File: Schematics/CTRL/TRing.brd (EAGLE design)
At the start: 94 x 49.2 mm, 39 parts

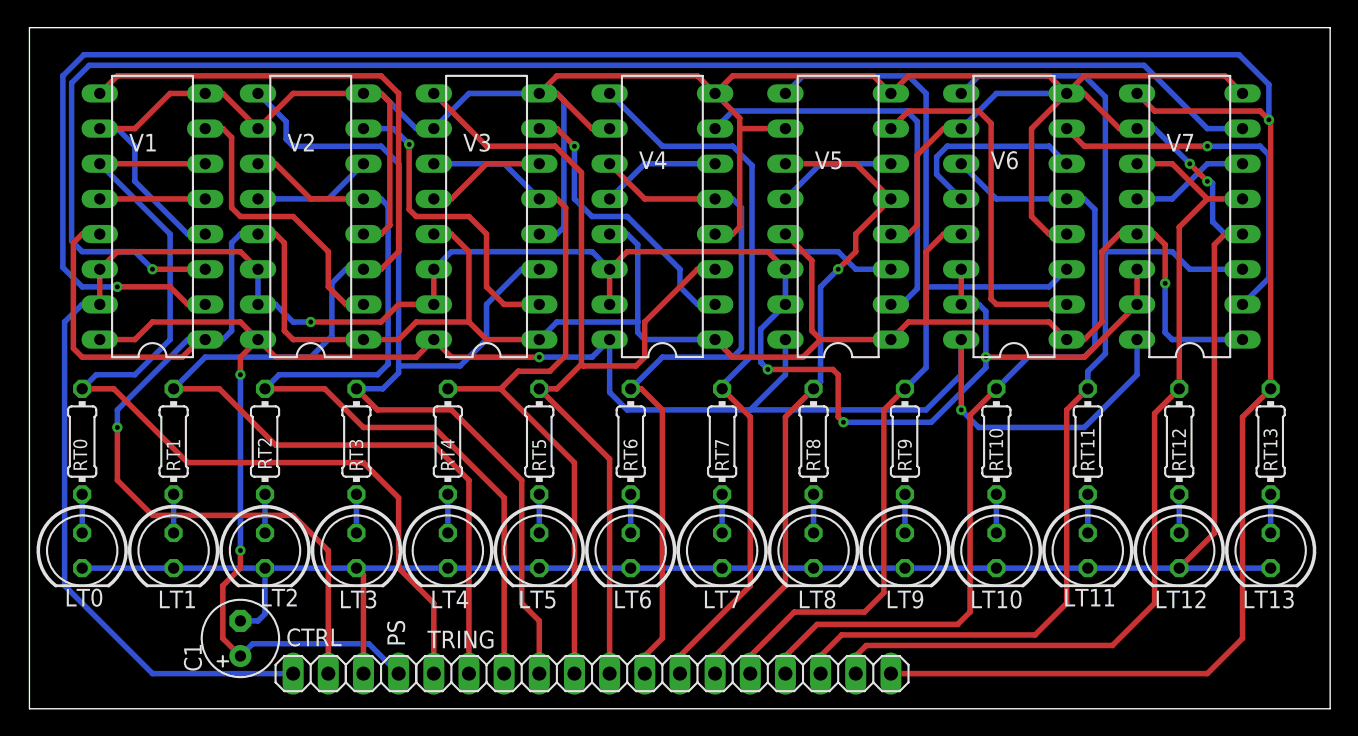
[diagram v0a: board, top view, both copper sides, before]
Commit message: Reduce Tring width
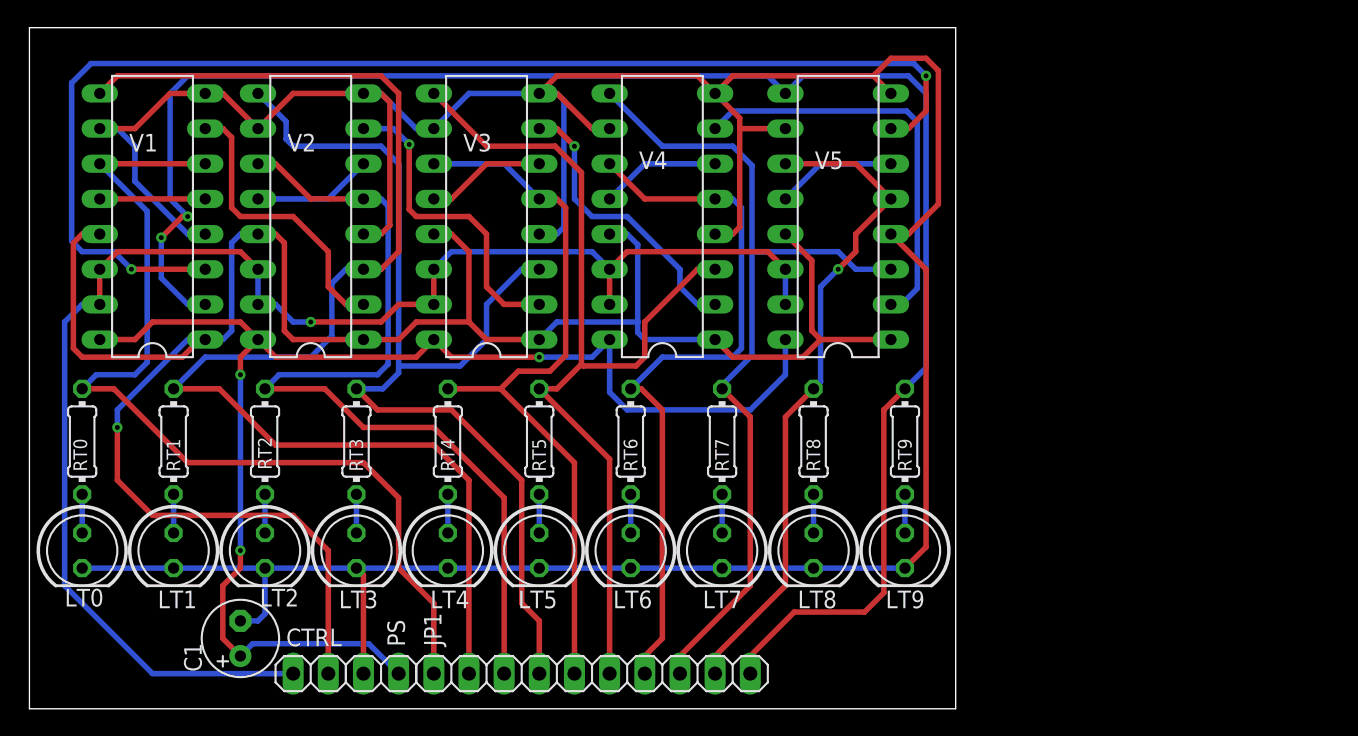
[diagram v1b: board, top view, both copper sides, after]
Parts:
- removed LT10, LT11, LT12, LT13: (no value), led:LED5MM
- removed RT10, RT11, RT12, RT13: (no value), rcl:0204/7
- removed TRING: (no value), pinhead:1X14
- removed V6, V7: 74112N, 74ttl-din:DIL16
- added JP1: (no value), pinhead:1X10
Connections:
- removed net !T13: V1.3, V7.7
- removed net N$12: V5.7, V6.2
- removed net N$14: V6.12, V6.6
- removed net N$20: LT10.A, RT10.1
- removed net N$21: LT11.A, RT11.1
- removed net N$22: V6.7, V7.2
- removed net N$24: LT12.A, RT12.1
- removed net N$25: V7.12, V7.6
- removed net N$26: LT13.A, RT13.1
- removed net T10: RT10.2, TRING.11, V6.11, V6.5
- removed net T11: RT11.2, TRING.12, V6.9, V7.3
- removed net T12: RT12.2, TRING.13, V7.11, V7.5
- removed net T13: RT13.2, TRING.14, V1.2, V7.9
- new net !T9: V1.3, V5.7
- net CLK: no longer V6.1, V6.13, V7.1, V7.13
- net CLR: no longer V6.14, V6.15, V7.14, V7.15
- net GND: no longer LT10.K, LT11.K, LT12.K, LT13.K, V6.10, V6.4, V6.8, V7.10, V7.4, V7.8
- net T0: now also JP1.10; no longer TRING.1
- net T1: now also JP1.9; no longer TRING.2
- net T2: now also JP1.8; no longer TRING.3
- net T3: now also JP1.7; no longer TRING.4
- net T4: now also JP1.6; no longer TRING.5
- net T5: now also JP1.5; no longer TRING.6
- net T6: now also JP1.4; no longer TRING.7
- net T7: now also JP1.3; no longer TRING.8
- net T8: now also JP1.2; no longer TRING.9
- net T9: now also JP1.1, V1.2; no longer TRING.10, V6.3
- net VCC: no longer V6.16, V7.16
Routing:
- net T13: track 191.5 -> 0.00 mm, vias 2 -> 0
- net !T13: track 108.9 -> 0.00 mm, vias 1 -> 0
- net !T9: track 0.00 -> 90.2 mm, vias 0 -> 2
- net GND: track 329.6 -> 242.9 mm, vias 2 -> 0
- net T11: track 80.4 -> 0.00 mm
- net T12: track 63.9 -> 0.00 mm
- net T10: track 62.1 -> 0.00 mm
- net T9: track 72.0 -> 125.7 mm, vias 0 -> 2
- net CLR: track 157.7 -> 107.7 mm, vias 4 -> 1
- net CLK: track 199.1 -> 151.5 mm, vias 2 -> 1
- net VCC: track 139.0 -> 97.7 mm, vias 4 -> 3
- net N$22: track 27.0 -> 0.00 mm, vias 1 -> 0
- net N$12: track 26.5 -> 0.00 mm
- net N$14: track 14.0 -> 0.00 mm
- net N$25: track 8.67 -> 0.00 mm
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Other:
- board size 94 x 49.2 mm -> 66.9 x 49.2 mm

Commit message: Changed order of LEDs and widht is now 11bits (0-10).
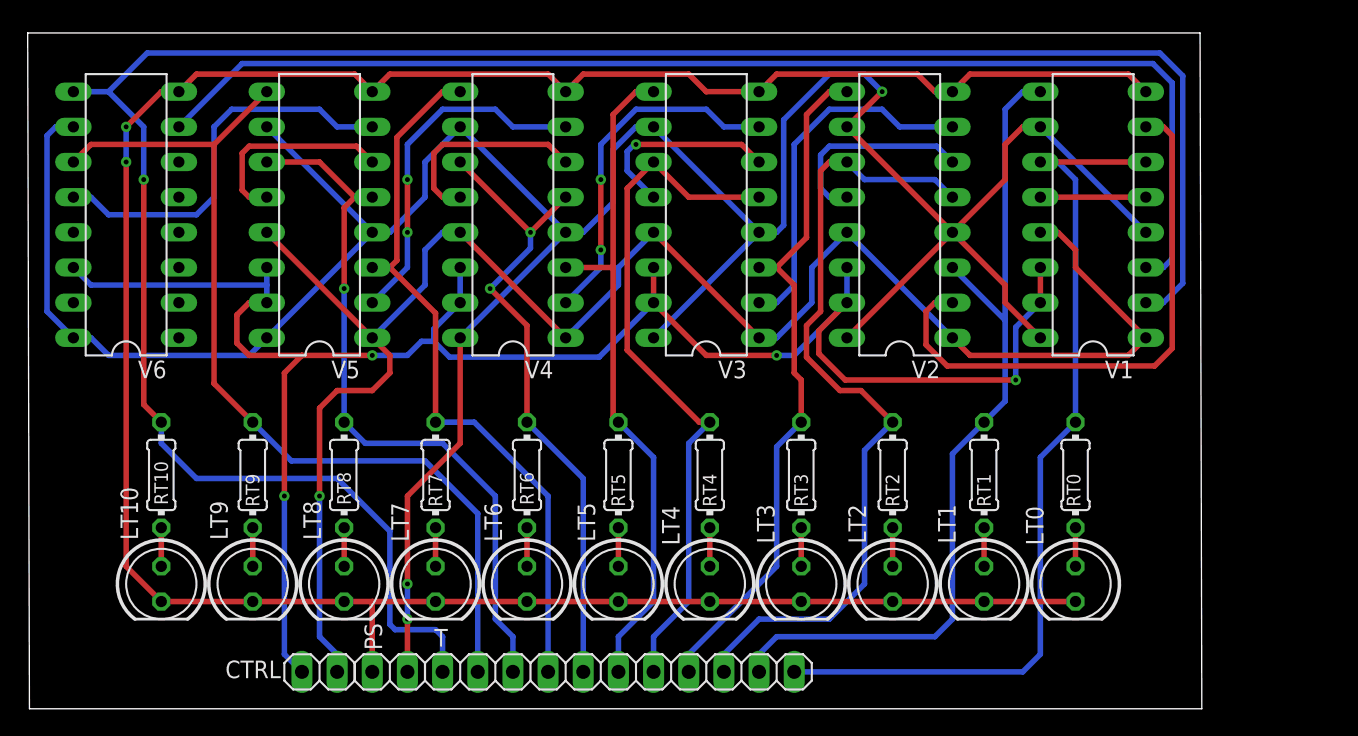
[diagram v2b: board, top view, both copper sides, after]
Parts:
- removed C1: (no value), rcl:E2,5-6
- removed JP1: (no value), pinhead:1X10
- added LT10: (no value), led:LED5MM
- added RT10: (no value), rcl:0204/7
- added T: (no value), pinhead:1X11
- added V6: 74112N, 74ttl-din:DIL16
- moved LT0 71.8 mm to (75.6, 9.02)
- moved RT0 71.8 mm to (75.6, 16.9)
- moved V1 67.9 mm to (76.8, 35.7)
- moved LT1 58.6 mm to (69.0, 9.02)
- moved RT1 58.6 mm to (69.0, 16.9)
- moved LT9 47.2 mm to (16.1, 9.02)
- moved RT9 47.2 mm to (16.1, 16.9)
- moved LT2 45.4 mm to (62.4, 9.02)
- moved RT2 45.4 mm to (62.4, 16.9)
- moved V2 42.5 mm to (62.9, 35.7)
- moved V5 37.5 mm to (21.0, 35.7)
- moved LT8 34.0 mm to (22.7, 9.02)
- moved RT8 34.0 mm to (22.7, 16.9)
- moved LT3 32.2 mm to (55.8, 9.02)
- moved RT3 32.2 mm to (55.8, 16.9)
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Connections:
- new net !T10: V1.3, V6.7
- new net N$12: LT10.A, RT10.1
- new net T10: RT10.2, T.1, V1.2, V6.9
- net !T9: now also V6.12; no longer V1.3
- net CLR: now also V6.14
- net GND: now also LT10.K, V6.8; no longer C1.-, V1.10, V1.4, V2.10, V2.4, V3.10, V3.4, V4.10, V4.4, V5.10, V5.4
- net T0: now also T.11; no longer JP1.10
- net T1: now also T.10; no longer JP1.9
- net T2: now also T.9; no longer JP1.8
- net T3: now also T.8; no longer JP1.7
- net T4: now also T.7; no longer JP1.6
- net T5: now also T.6; no longer JP1.5
- net T6: now also T.5; no longer JP1.4
- net T7: now also T.4; no longer JP1.3
- net T8: now also T.3; no longer JP1.2
- net T9: now also T.2, V6.11; no longer JP1.1, V1.2
- net VCC: now also V1.10, V1.4, V2.10, V2.4, V3.10, V3.4, V4.10, V4.4, V5.10, V5.4, V6.10, V6.16; no longer C1.+
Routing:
- net T10: track 0.00 -> 159.8 mm, vias 0 -> 1
- net VCC: track 97.7 -> 221.5 mm
- net !T10: track 0.00 -> 89.1 mm
- net !T9: track 90.2 -> 28.8 mm, vias 2 -> 0
- net T9: track 125.7 -> 67.7 mm, vias 2 -> 0
- net GND: track 242.9 -> 186.4 mm, vias 0 -> 2
- net T1: track 94.7 -> 63.2 mm
- net CLR: track 107.7 -> 135.2 mm, vias 1 -> 4
- net T3: track 75.4 -> 50.1 mm
- net CLK: track 151.5 -> 130.7 mm
- net N$5: track 21.2 -> 41.1 mm
- net T5: track 67.4 -> 49.6 mm
- net T7: track 63.5 -> 52.4 mm
- net N$19: track 8.67 -> 15.0 mm
- net T6: track 52.7 -> 46.5 mm, vias 0 -> 2
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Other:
- board size 66.9 x 49.2 mm -> 84.8 x 48.8 mm

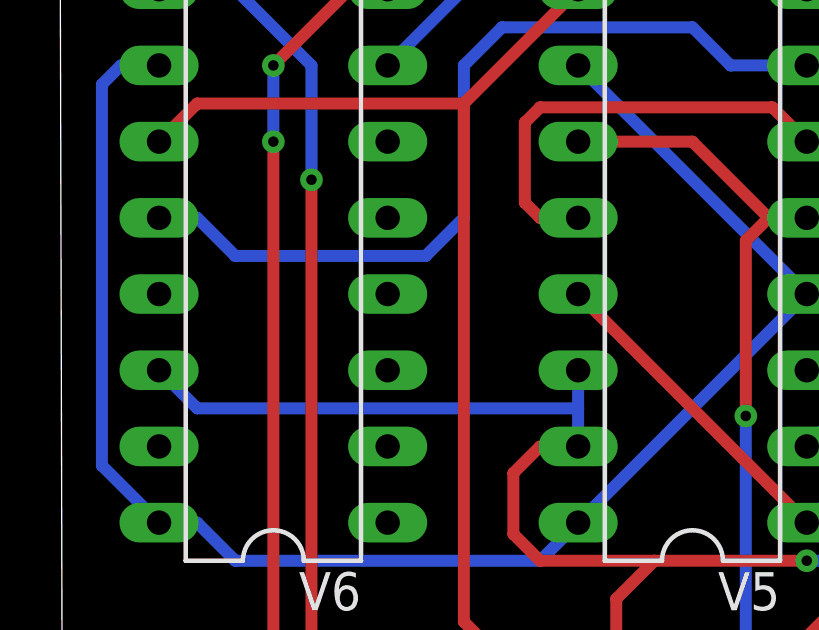
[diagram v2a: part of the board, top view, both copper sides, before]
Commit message: Fixed 2 problems, that I found after ordering boards
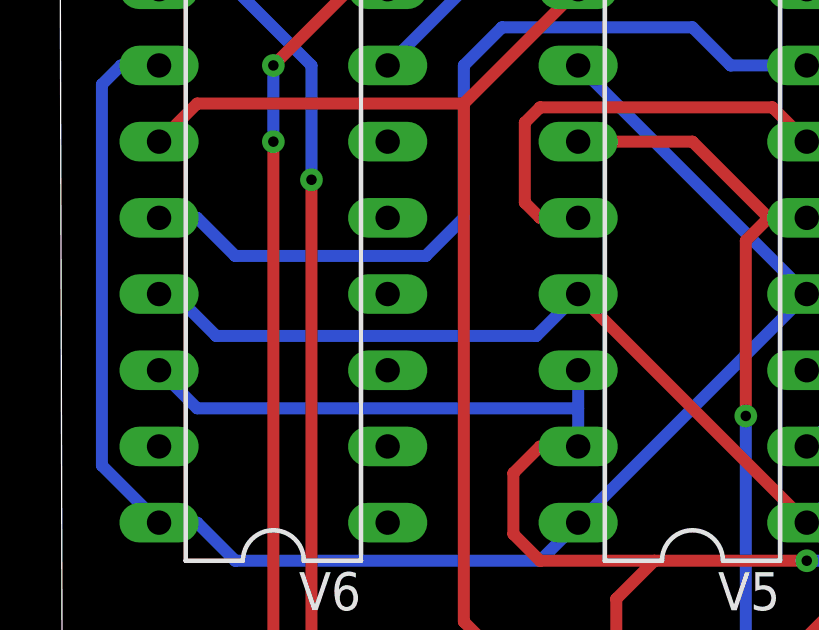
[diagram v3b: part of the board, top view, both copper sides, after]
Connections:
- net CLK: now also V6.13
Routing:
- net CLK: track 130.7 -> 145.8 mm
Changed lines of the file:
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@@
 <wire x1="56.515" y1="29.337" x2="53.975" y2="26.797" width="0.4" layer="16"/>
 <wire x1="53.975" y1="26.797" x2="52.705" y2="26.797" width="0.4" layer="16"/>
+<contactref element="V6" pad="13"/>
+<wire x1="3.175" y1="34.417" x2="3.683" y2="34.417" width="0.4" layer="16"/>
+<wire x1="3.683" y1="34.417" x2="5.08" y2="33.02" width="0.4" layer="16"/>
+<wire x1="15.748" y1="33.02" x2="17.145" y2="34.417" width="0.4" layer="16"/>
+<wire x1="5.08" y1="33.02" x2="15.748" y2="33.02" width="0.4" layer="16"/>
 </signal>
 <signal name="!T8">
